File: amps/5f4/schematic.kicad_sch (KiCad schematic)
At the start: 66 parts, among them T3 45216

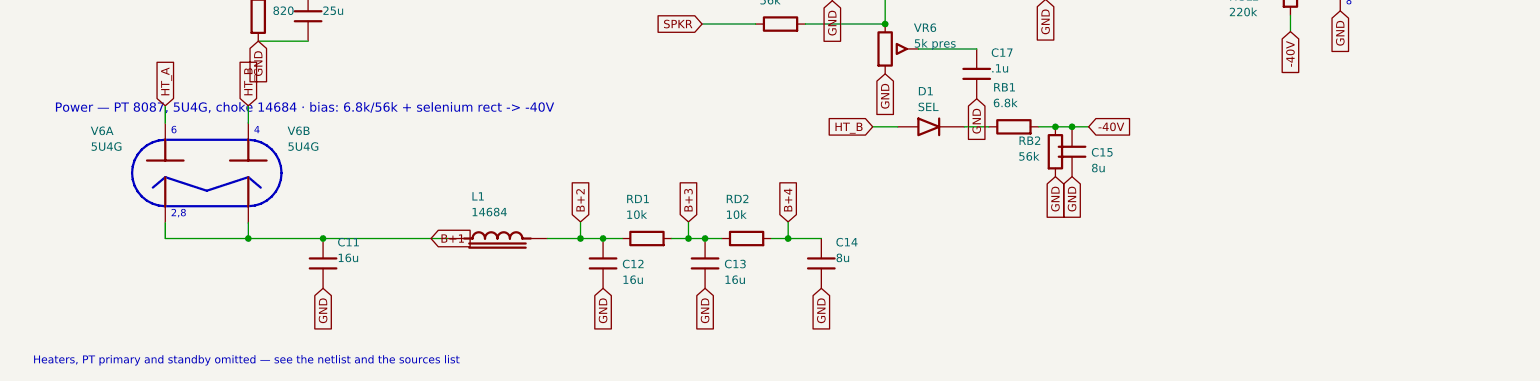
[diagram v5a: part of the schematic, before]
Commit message: Fix: feed the tweed bias rectifiers from the transformer's bias tap, not a rectifier plate (5E4-A, 5E5-A, 5F4, 5G9)
The 8087-family power transformer brings out a BIAS TAP on the HT winding,
between one end and the centre tap — the layouts letter that lead RED-BLUE
— and every fixed-bias tweed factory sheet draws the bias rectifier from
that fourth winding terminal. These four sheets drew it from a rectifier
plate (the HT_B label). The boards carry the same mistake, which is why the
sheet-vs-board gate could not see it; the source read did.

cx:PT gains an OPTIONAL pin 6, HT_TAP, between HT_A and the centre tap.
`s.pt(..., tap=True)` asks for it, and only that sheet's embedded library
carries the pin (lib_text(pt_tap=...)), so every sheet that does not wire
it is byte-identical — proved by the regenerate-all diff below. The
contract tables (SYM_EXTENTS/SYM_PINS) are built with the pin so the lint
and the wire-cutting know it; the tap lies inside the symbol's box, so no
extent moves.

- 5g9: T1 8160 drawn with the tap (moved 8 mm left for the label), the
  selenium rectifier's AC side on HT_TAP (crop 5g9-D1-schem.png: the
  rectifier + runs straight to a winding terminal between the 300 V AC end
  and the centre tap; layout: a separate lead to SEL. RECT. +).
- 5e4a, 5f4: these sheets drew no PT at all, so a T1 is added (MAINS labels
  on the primary, HT_A / HT_TAP / centre tap / HT_B on the secondary, the
  same idiom the 5G9 uses), the 18k / 6800 bias feed taken from HT_TAP,
  and T1 added to bom.yaml (crops 5e4a-D1-schem.png, 5f4-D1-schem.png:
  the series resistor from a winding terminal between the top end and the
  centre tap; 5e4a-D1-layout.png: RED-BLUE lead to the selenium +).
- 5e5a: T1 added the same way; the bias row now carries the factory's 10 K
  in series from the tap into the cell and the 56 K bleeder across the
  100 µF can (crop 5e5a-D1-schem.png), both added to bom.yaml (RB1, RB2)
  — the board places neither, so they report SHEET-ONLY until it doe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
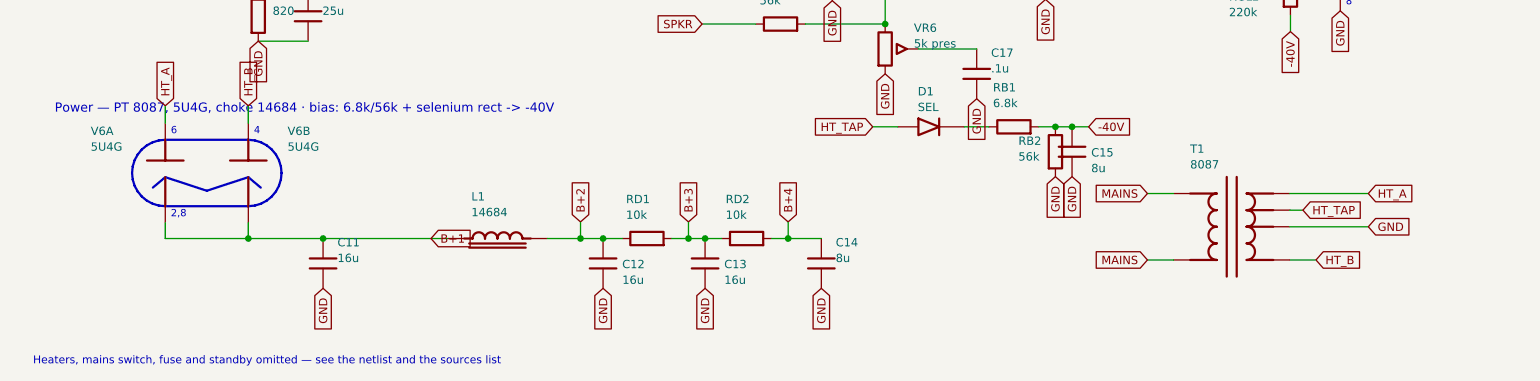
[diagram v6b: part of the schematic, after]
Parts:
- added T1: 8087, symbol cx:PT
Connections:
- net GND: now also T1.4 (HT_CT)
- net HT_A: now also T1.3 (HT_A)
- net HT_B: now also T1.5 (HT_B); no longer D1.1 (A)
- new net HT_TAP: D1.1 (A), T1.6 (HT_TAP)
- new net MAINS: T1.1 (PRI_1), T1.2 (PRI_2)
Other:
- note added: "Heaters, mains switch, fuse and standby omitted — see the netlist and the sources list"
- note removed: "Heaters, PT primary and standby omitted — see the netlist and the sources list"
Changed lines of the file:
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@@
   (global_label "GND" (shape input) (at 133.258 131.698 270)
     (effects (font (size 1.27 1.27)) (justify right)))
-  (global_label "HT_B" (shape input) (at 141.118 106.998 180)
+  (global_label "HT_TAP" (shape input) (at 141.118 106.998 180)
     (effects (font (size 1.27 1.27)) (justify right)))
   (wire (pts (xy 141.118 106.998) (xy 144.928 106.998))
@@
     (effects (font (size 1.27 1.27)) (justify right)))
   (global_label "-40V" (shape input) (at 174.138 106.998 0)
+    (effects (font (size 1.27 1.27)) (justify left)))
+  (symbol (lib_id "cx:PT") (at 196.018 122.278 0) (unit 1)
+    (in_bom yes) (on_board yes)
+    (property "Reference" "T1" (at 189.668 110.378 0) (effects (font (size 1.27 1.27)) (justify left)))
+    (property "Value" "8087" (at 189.668 112.778 0) (effects (font (size 1.27 1.27)) (justify left))))
+  (wire (pts (xy 187.128 117.198) (xy 183.128 117.198))
+    (stroke (width 0) (type default)))
+  (global_label "MAINS" (shape input) (at 183.128 117.198 180)
+    (effects (font (size 1.27 1.27)) (justify right)))
+  (wire (pts (xy 187.128 127.358) (xy 183.128 127.358))
+    (stroke (width 0) (type default)))
+  (global_label "MAINS" (shape input) (at 183.128 127.358 180)
+    (effects (font (size 1.27 1.27)) (justify right)))
+  (wire (pts (xy 204.908 117.198) (xy 216.908 117.198))
+    (stroke (width 0) (type default)))
+  (global_label "HT_A" (shape input) (at 216.908 117.198 0)
+    (effects (font (size 1.27 1.27)) (justify left)))
+  (wire (pts (xy 204.908 119.738) (xy 206.908 119.738))
+    (stroke (width 0) (type default)))
+  (global_label "HT_TAP" (shape input) (at 206.908 119.738 0)
+    (effects (font (size 1.27 1.27)) (justify left)))
+  (wire (pts (xy 204.908 122.278) (xy 216.908 122.278))
+    (stroke (width 0) (type default)))
+  (global_label "GND" (shape input) (at 216.908 122.278 0)
+    (effects (font (size 1.27 1.27)) (justify left)))
+  (wire (pts (xy 204.908 127.358) (xy 208.908 127.358))
+    (stroke (width 0) (type default)))
+  (global_label "HT_B" (shape input) (at 208.908 127.358 0)
     (effects (font (size 1.27 1.27)) (justify left)))
   (polyline (pts (xy 45.628 108.978) (xy 46.619 109.076) (xy 47.572 109.365) (xy 48.45 109.834) (xy 49.22 110.466) (xy 49.852 111.236) (xy 50.321 112.114) (xy 50.61 113.067) (xy 50.708 114.058) (xy 50.61 115.049) (xy 50.321 116.002) (xy 49.852 116.88) (xy 49.22 117.65) (xy 48.45 118.282) (xy 47.572 118.751) (xy 46.619 119.04) (xy 45.628 119.138) (xy 32.928 119.138) (xy 31.937 119.04) (xy 30.984 118.751) (xy 30.106 118.282) (xy 29.336 117.65) (xy 28.704 116.88) (xy 28.235 116.002) (xy 27.946 115.049) (xy 27.848 114.058) (xy 27.946 113.067) (xy 28.235 112.114) (xy 28.704 111.236) (xy 29.336 110.466) (xy 30.106 109.834) (xy 30.984 109.365) (xy 31.937 109.076) (xy 32.928 108.978) (xy 45.628 108.978))
@@
   (text "4" (at 46.478 107.708 0)
     (effects (font (size 1.1 1.1)) (justify left)))
-  (text "Heaters, PT primary and standby omitted — see the netlist and the sources list" (at 12.7 142.856 0)
+  (text "Heaters, mains switch, fuse and standby omitted — see the netlist and the sources list" (at 12.7 142.856 0)
     (effects (font (size 1.2 1.2)) (justify left)))
   (sheet_instances (path "/" (page "1")))

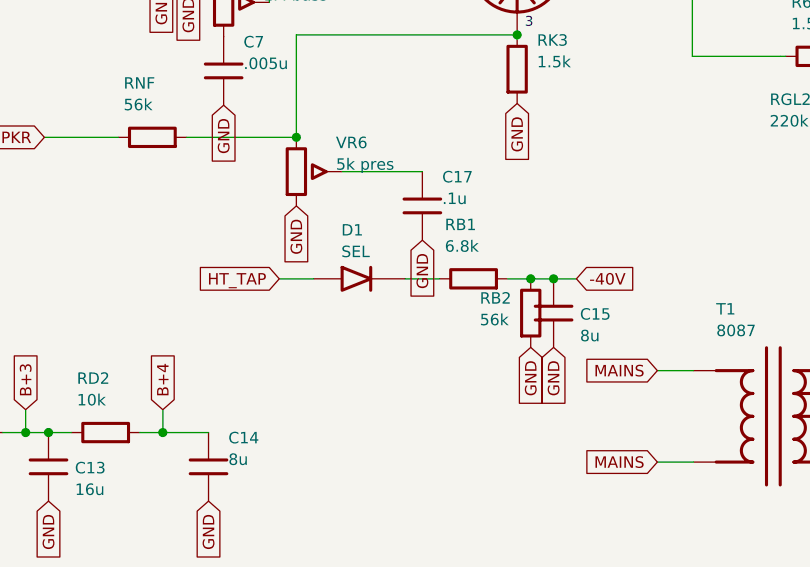
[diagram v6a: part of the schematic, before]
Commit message: Fix: six sheets letter valve sections and bias rows the way their factory drawings do
Sections — the board was right and the sheet printed the other half's pin
numbers (triage verdict rows, crops under the triage scratch):
  AC30 V1    JMI OS/065 (3600x2492): Brilliant grid 2 / plate 1, Normal 7 / 6
  AA964 V1   input 2/1/3, second stage 7/6/8 (6322x3926)
  AA964 V2   phase inverter 7/6/8, tremolo oscillator 2/1/3
  5F6-A V3   the 82k (input) triode on 1/2/3 on the I-EG layout (6402x3641)
  6G4 V5     the 82k triode on 1/2/3 on the A-FJ layout (2250x1269, the only copy)

Bias rows — the 5F4 (C-EG) and 5E4-A (G-EE) drawings run the series
resistor (6800 / 18K) from the transformer's bias tap INTO the selenium
rectifier. The previous commit's rows put the rectifier on the tap and the
resistor after it; both now read tap -> resistor -> rectifier -> node. The
5F4 rectifier sits clear of C17's ground flag.

Worklist after re-export: section swaps 10 -> 5 (three board re-pins in
flight, the 5E5-A whose only copy does not resolve, and the AA1164 V4 still
being read); the 5F4/5E4-A D1 rows stay MISPLACED until their boards take
the tap lead, which the board repair wave is adding.

Gates: check_schematics 40/0 (+selftest), verify_schematic_nets 40 clean,
tone gate, validate, check_value_consistency --strict 0, test_era_values,
verify_sheet_vs_board selftest 19 + drift clean after --export,
check_heaters, verify_layout_nets; regenerating every sheet changes only
these six.

Co-Authored-By: Claude Opus 5 (1M context) <noreply@anthropic.com>
Claude-Session: https://claude.ai/code/session_01KBMfdh37HmCL2iWcBiL5J1
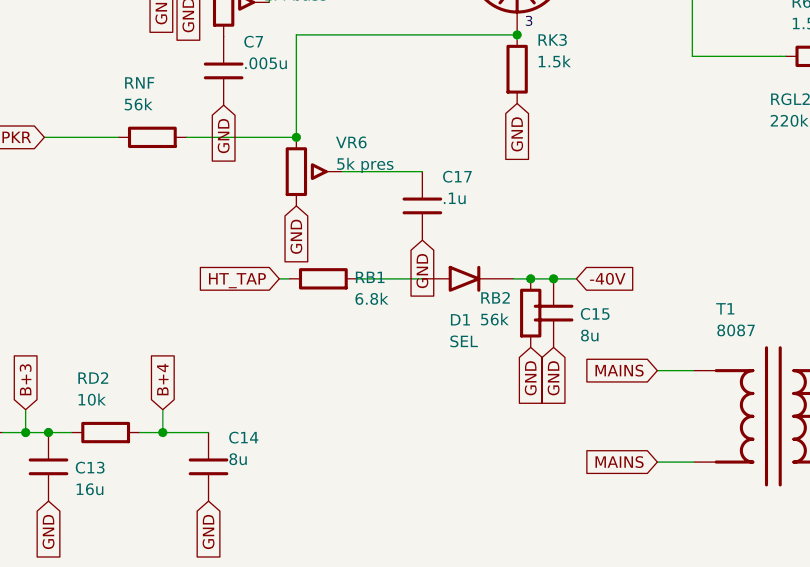
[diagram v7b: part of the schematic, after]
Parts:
- removed D1: SEL, symbol cx:DIODE_SS
- added RB1: 6.8k, symbol cx:R
- D1: renamed from RB1; value 6.8k -> SEL; symbol cx:R -> cx:DIODE_SS
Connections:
- net HT_TAP: now also RB1.1
- net at D1.1 (A): now also RB1.2
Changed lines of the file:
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@@
   (global_label "HT_TAP" (shape input) (at 141.118 106.998 180)
     (effects (font (size 1.27 1.27)) (justify right)))
-  (wire (pts (xy 141.118 106.998) (xy 144.928 106.998))
+  (symbol (lib_id "cx:R") (at 146.018 106.998 90) (unit 1)
+    (in_bom yes) (on_board yes)
+    (property "Reference" "RB1" (at 149.458 106.882 270) (effects (font (size 1.27 1.27)) (justify left)))
+    (property "Value" "6.8k" (at 149.458 109.282 270) (effects (font (size 1.27 1.27)) (justify left))))
+  (wire (pts (xy 141.118 106.998) (xy 142.208 106.998))
     (stroke (width 0) (type default)))
-  (symbol (lib_id "cx:DIODE_SS") (at 150.008 106.998 0) (unit 1)
+  (wire (pts (xy 149.828 106.998) (xy 156.938 106.998))
+    (stroke (width 0) (type default)))
+  (symbol (lib_id "cx:DIODE_SS") (at 162.018 106.998 0) (unit 1)
     (in_bom yes) (on_board yes)
-    (property "Reference" "D1" (at 148.008 101.598 0) (effects (font (size 1.27 1.27)) (justify left)))
-    (property "Value" "SEL" (at 148.008 103.998 0) (effects (font (size 1.27 1.27)) (justify left))))
-  (wire (pts (xy 155.088 106.998) (xy 158.898 106.998))
-    (stroke (width 0) (type default)))
-  (symbol (lib_id "cx:R") (at 162.708 106.998 90) (unit 1)
-    (in_bom yes) (on_board yes)
-    (property "Reference" "RB1" (at 159.508 100.998 270) (effects (font (size 1.27 1.27)) (justify left)))
-    (property "Value" "6.8k" (at 159.508 103.398 270) (effects (font (size 1.27 1.27)) (justify left))))
-  (wire (pts (xy 158.898 106.998) (xy 158.898 106.998))
-    (stroke (width 0) (type default)))
-  (wire (pts (xy 166.518 106.998) (xy 169.058 106.998))
+    (property "Reference" "D1" (at 160.018 111.598 0) (effects (font (size 1.27 1.27)) (justify left)))
+    (property "Value" "SEL" (at 160.018 113.998 0) (effects (font (size 1.27 1.27)) (justify left))))
+  (wire (pts (xy 167.098 106.998) (xy 169.058 106.998))
     (stroke (width 0) (type default)))
   (wire (pts (xy 169.058 106.998) (xy 171.598 106.998))

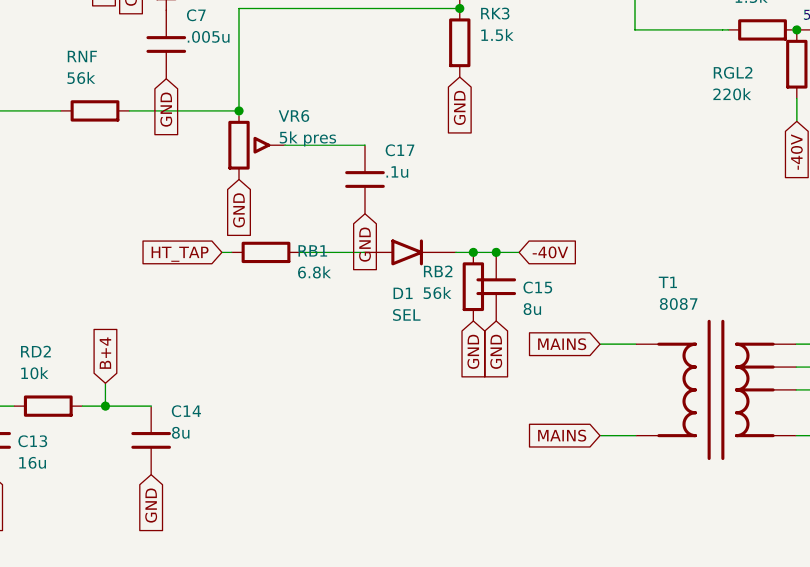
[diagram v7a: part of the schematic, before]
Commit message: Fix: 17 bias rectifiers and six HT diodes drawn backwards; the 6G6-B and 6G4 bias rows as their drawings show; AA1164 V4 units
Rectifier polarity has no gate. The netlists model every supply as an ideal
source, the sheet-vs-board check treats a two-terminal part as unordered, and
the boards' `cathode:` fields were copied from the sheets. Measured over all
68 diodes on 40 sheets: 18 negative-bias rectifiers had the cathode on the
negative node (a diode that way round would charge the node POSITIVE), and all
six 6G6-B HT diodes pointed away from B+. The printed negative bias on each of
those sheets falsifies the drawn orientation; the nine bias rectifiers already
right (AA1164, AA864, AB165, B15N, DR103, JTM100, M1959, M2204, 6G6-B) show
the idiom. Flipped: 5E4-A, 5E5-A, 5E6-A, 5F10, 5F4, 5F6, 5F6-A, 5F8-A, 5G9,
6G2, 6G3, 6G4, 6G5, AA964, AB763, AB763 Super, AB763 Twin, JTM45 (the
M1987's is with the Marshall board repair) and the 6G6-B's DR1-DR6. The
5F8-A board, which had copied its sheet, has the band moved to the tap side;
the other boards' bands are with the board-repair wave. A gate is next.

6G6-B bias. E-FB (6431x3364): the 1K 1W rises from TR1's SECOND secondary
terminal, a bias tap between the upper HT end and the grounded centre tap,
to the diode's + end. The sheet fed the diode from the HT end with the 1K
after it. T1 now carries its tap pin and the row reads tap -> 1K -> diode ->
-54 V. (The triage had read "HT end"; the native crop shows the tap.)

6G4 bias. A-FJ, read natively: tap -> rectifier -> 8 uF -> 10K -> the -55 V
node, which carries a second 8 uF and the 56K to ground as a bleeder. The
sheet fed the rectifier from an HT end, drew the 56K in series and carried
one capacitor. CBIAS2 joins the parts list, and RBIAS1's role now says
bleeder.

AA1164 V4. The K-FD sheet prints the phase inverter 7/6/8 and the tremolo
oscillator 2/1/3 (5554x4346); the sheet had them the other way round.

Gates: check_schematics 40/0 (+selftest), verify_schematic_nets 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
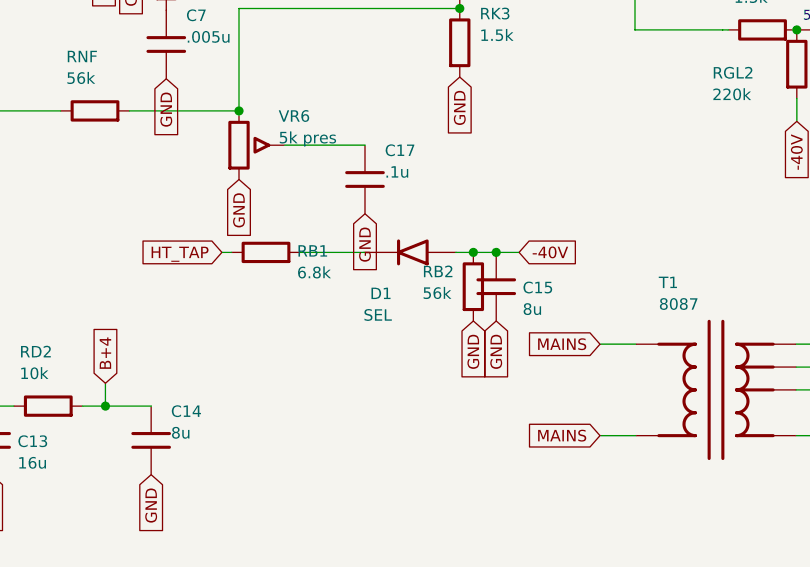
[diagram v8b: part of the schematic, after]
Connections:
- net -40V: now also D1.1 (A); no longer D1.2 (K)
- net at RB1.2: now also D1.2 (K); no longer D1.1 (A)
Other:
- moved on the sheet: D1
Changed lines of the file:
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@@
   (wire (pts (xy 149.828 106.998) (xy 156.938 106.998))
     (stroke (width 0) (type default)))
-  (symbol (lib_id "cx:DIODE_SS") (at 162.018 106.998 0) (unit 1)
+  (symbol (lib_id "cx:DIODE_SS") (at 162.018 106.998 180) (unit 1)
     (in_bom yes) (on_board yes)
     (property "Reference" "D1" (at 160.018 111.598 0) (effects (font (size 1.27 1.27)) (justify left)))
